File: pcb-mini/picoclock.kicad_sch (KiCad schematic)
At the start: 83 parts, among them J1 UART, J10 USB, J11 Alt Power, J12 LED_5V, J14 SJ2-35863B1-SMT-TR, J2 USB_A, J3 UART, J4 xx, J5 Micro_SD_Card_Det1, J6 USB_C_Receptacle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

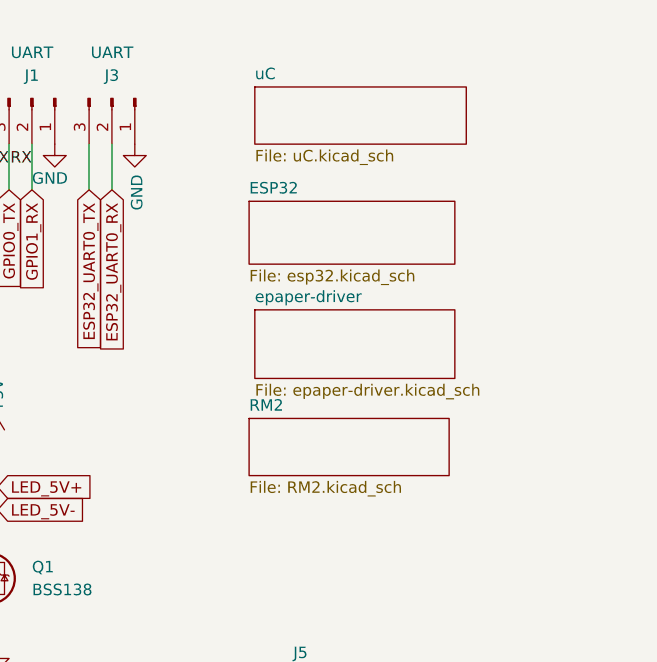
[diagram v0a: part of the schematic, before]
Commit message: [pcb] mini: add debug port, improve/fix traces
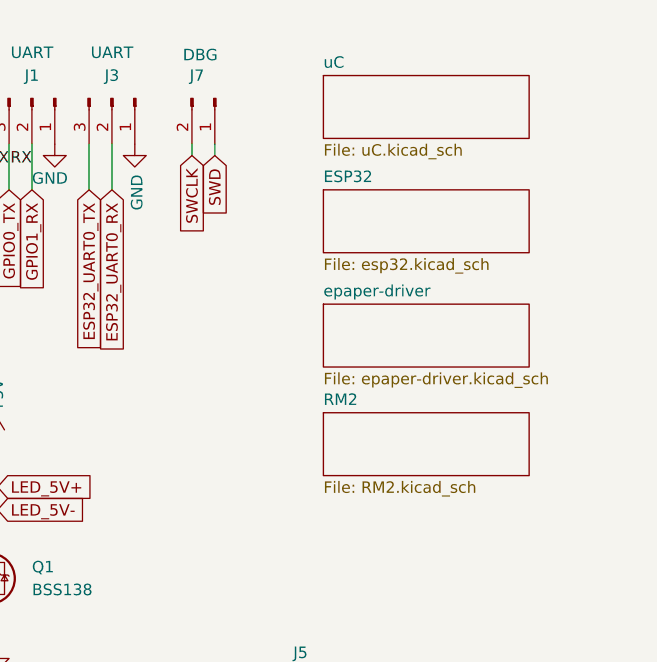
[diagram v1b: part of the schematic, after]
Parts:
- added J7: DBG, Connector_PinHeader_2.54mm:PinHeader_1x02_P2.54mm_Vertical, symbol Connector:Conn_01x02_Pin
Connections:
- new net SWCLK: J7.2 (Pin_2)
- new net SWD: J7.1 (Pin_1)
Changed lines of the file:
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@@
 	(wire
 		(pts
+			(xy 243.84 27.94) (xy 243.84 26.67)
+		)
+		(stroke
+			(width 0)
+			(type default)
+		)
+	)
+	(wire
+		(pts
 			(xy 31.75 166.37) (xy 31.75 171.45)
 		)
@@
 	(wire
 		(pts
+			(xy 241.3 27.94) (xy 241.3 26.67)
+		)
+		(stroke
+			(width 0)
+			(type default)
+		)
+	)
+	(wire
+		(pts
 			(xy 31.242 117.856) (xy 35.687 117.856)
 		)
@@
 		)
 	)
+	(global_label "SWCLK"
+		(shape input)
+		(at 241.3 27.94 270)
+		(fields_autoplaced yes)
+		(effects
+			(font
+				(size 1.27 1.27)
+			)
+			(justify right)
+		)
+		(property "Intersheetrefs" "${INTERSHEET_REFS}"
+			(at 241.3 37.1542 90)
+			(effects
+				(font
+					(size 1.27 1.27)
+				)
+				(justify right)
+				(hide yes)
+			)
+		)
+	)
 	(global_label "SDA"
 		(shape input)
@@
 		)
 	)
+	(global_label "SWD"
+		(shape input)
+		(at 243.84 27.94 270)
+		(fields_autoplaced yes)
+		(effects
+			(font
+				(size 1.27 1.27)
+			)
+			(justify right)
+		)
+		(property "Intersheetrefs" "${INTERSHEET_REFS}"
+			(at 243.84 34.8561 90)
+			(effects
+				(font
+					(size 1.27 1.27)
+				)
+				(justify right)
+				(hide yes)
+			)
+		)
+	)
 	(global_label "GPIO28{slash}btn"
 		(shape input)
@@
 	)
 	(symbol
+		(lib_id "Connector:Conn_01x02_Pin")
+		(at 243.84 21.59 270)
+		(unit 1)
+		(exclude_from_sim no)
+		(in_bom yes)
+		(on_board yes)
+		(dnp no)
+		(property "Reference" "J7"
+			(at 241.046 19.05 90)
+			(effects
+				(font
+					(size 1.27 1.27)
+				)
+				(justify left)
+			)
+		)
+		(property "Value" "DBG"
+			(at 240.284 16.764 90)
+			(effects
+				(font
+					(size 1.27 1.27)
+				)
+				(justify left)
+			)
+		)
+		(property "Footprint" "Connector_PinHeader_2.54mm:PinHeader_1x02_P2.54mm_Vertical"
+			(at 243.84 21.59 0)
+			(effects
+				(font
+					(size 1.27 1.27)
+				)
+				(hide yes)
+			)
+		)
+		(property "Datasheet" "~"
+			(at 243.84 21.59 0)
+			(effects
+				(font
+					(size 1.27 1.27)
+				)
+				(hide yes)
+			)
+		)
+		(property "Description" ""
+			(at 243.84 21.59 0)
+			(effects
+				(font
+					(size 1.27 1.27)
+				)
+				(hide yes)
+			)
+		)
+		(pin "1"
+		)
+		(pin "2"
+		)
+		(instances
+			(project "picoclock"
+				(path "/3b9dec0e-e0b7-4565-afc9-c4692f41aea9"
+					(reference "J7")
+					(unit 1)
+				)
+			)
+		)
+	)
+	(symbol
 		(lib_id "power:GND")
 		(at 76.327 107.696 90)
@@
 	)
 	(sheet
-		(at 247.65 33.02)
+		(at 255.905 31.75)
 		(size 22.86 6.985)
 		(exclude_from_sim no)
@@
 		)
 		(property "Sheetname" "ESP32"
-			(at 247.65 32.3084 0)
+			(at 255.905 31.0384 0)
 			(effects
 				(font
@@
 		)
 		(property "Sheetfile" "esp32.kicad_sch"
-			(at 247.65 40.5896 0)
+			(at 255.905 39.3196 0)
 			(effects
 				(font
@@
 	)
 	(sheet
-		(at 248.285 45.085)
-		(size 22.225 7.62)
+		(at 255.905 44.45)
+		(size 22.86 6.985)
 		(exclude_from_sim no)
 		(in_bom yes)
@@
 		)
 		(property "Sheetname" "epaper-driver"
-			(at 248.285 44.3734 0)
+			(at 255.905 43.7384 0)
 			(effects
 				(font
@@
 		)
 		(property "Sheetfile" "epaper-driver.kicad_sch"
-			(at 248.285 53.2896 0)
+			(at 255.905 52.0196 0)
 			(effects
 				(font
@@
 	)
 	(sheet
-		(at 247.65 57.15)
-		(size 22.225 6.35)
+		(at 255.905 56.515)
+		(size 22.86 6.985)
 		(exclude_from_sim no)
 		(in_bom yes)
@@
 		)
 		(property "Sheetname" "RM2"
-			(at 247.65 56.4384 0)
+			(at 255.905 55.8034 0)
 			(effects
 				(font
@@
 		)
 		(property "Sheetfile" "RM2.kicad_sch"
-			(at 247.65 64.0846 0)
+			(at 255.905 64.0846 0)
 			(effects
 				(font
@@
 	)
 	(sheet
-		(at 248.285 20.32)
-		(size 23.495 6.35)
+		(at 255.905 19.05)
+		(size 22.86 6.985)
 		(exclude_from_sim no)
 		(in_bom yes)
@@
 		)
 		(property "Sheetname" "uC"
-			(at 248.285 19.6084 0)
+			(at 255.905 18.3384 0)
 			(effects
 				(font
@@
 		)
 		(property "Sheetfile" "uC.kicad_sch"
-			(at 248.285 27.2546 0)
+			(at 255.905 26.6196 0)
 			(effects
 				(font

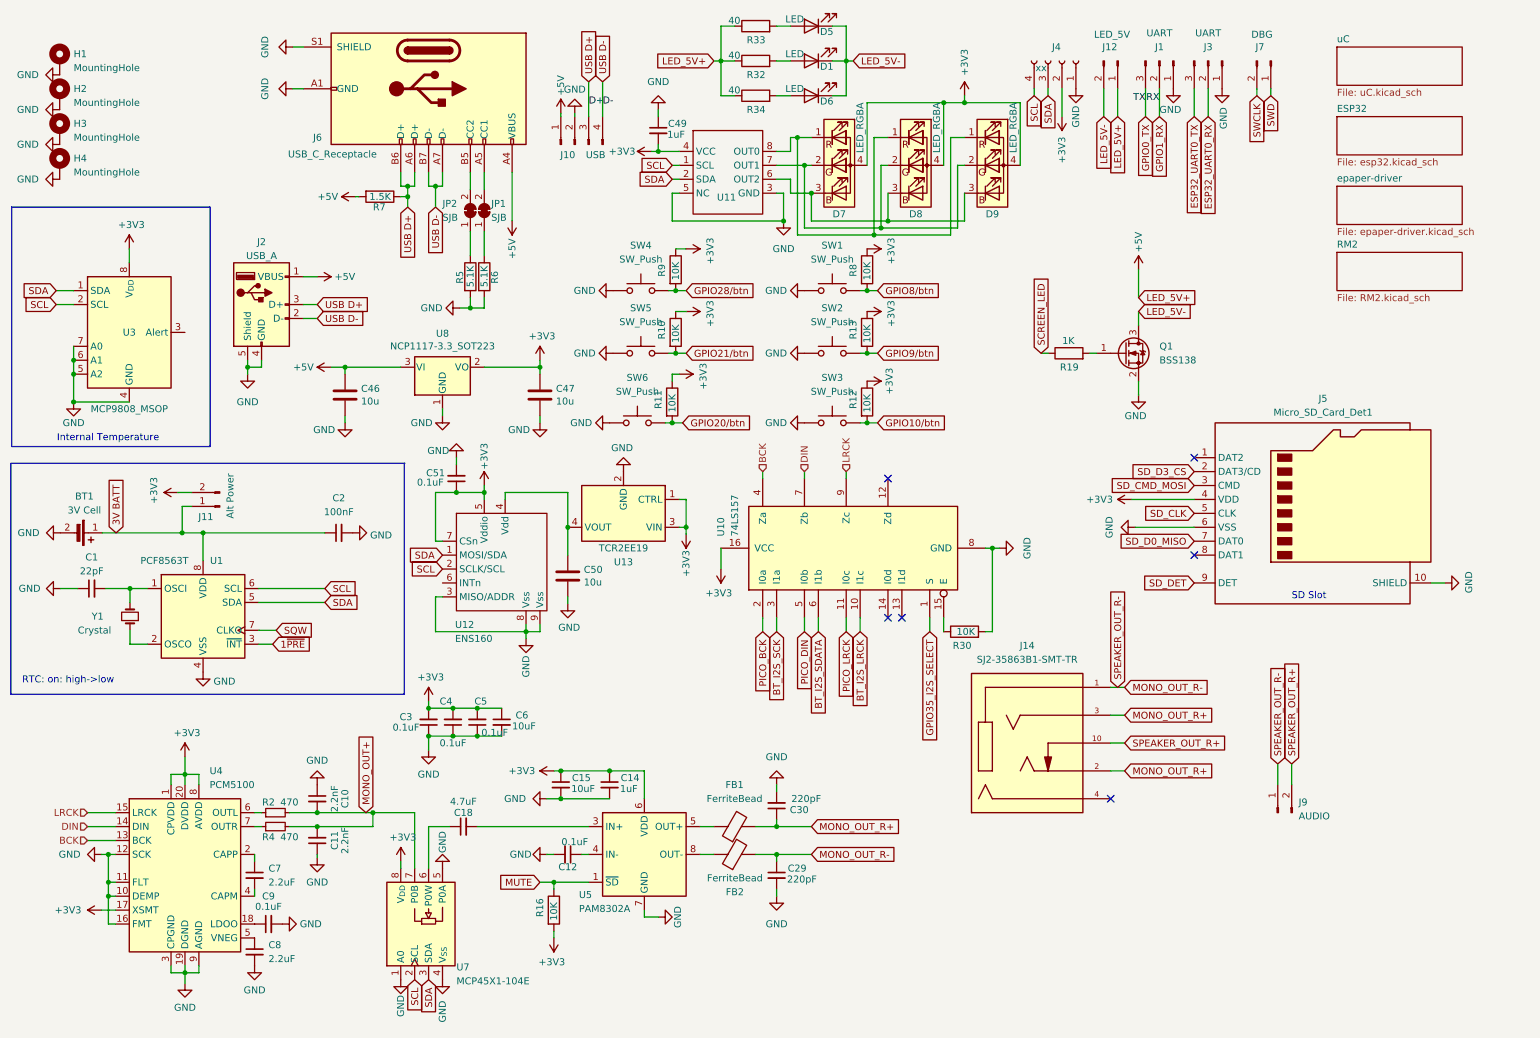
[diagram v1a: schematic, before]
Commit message: [pcb] mini: cleanup schematic, fix 3.3v zone
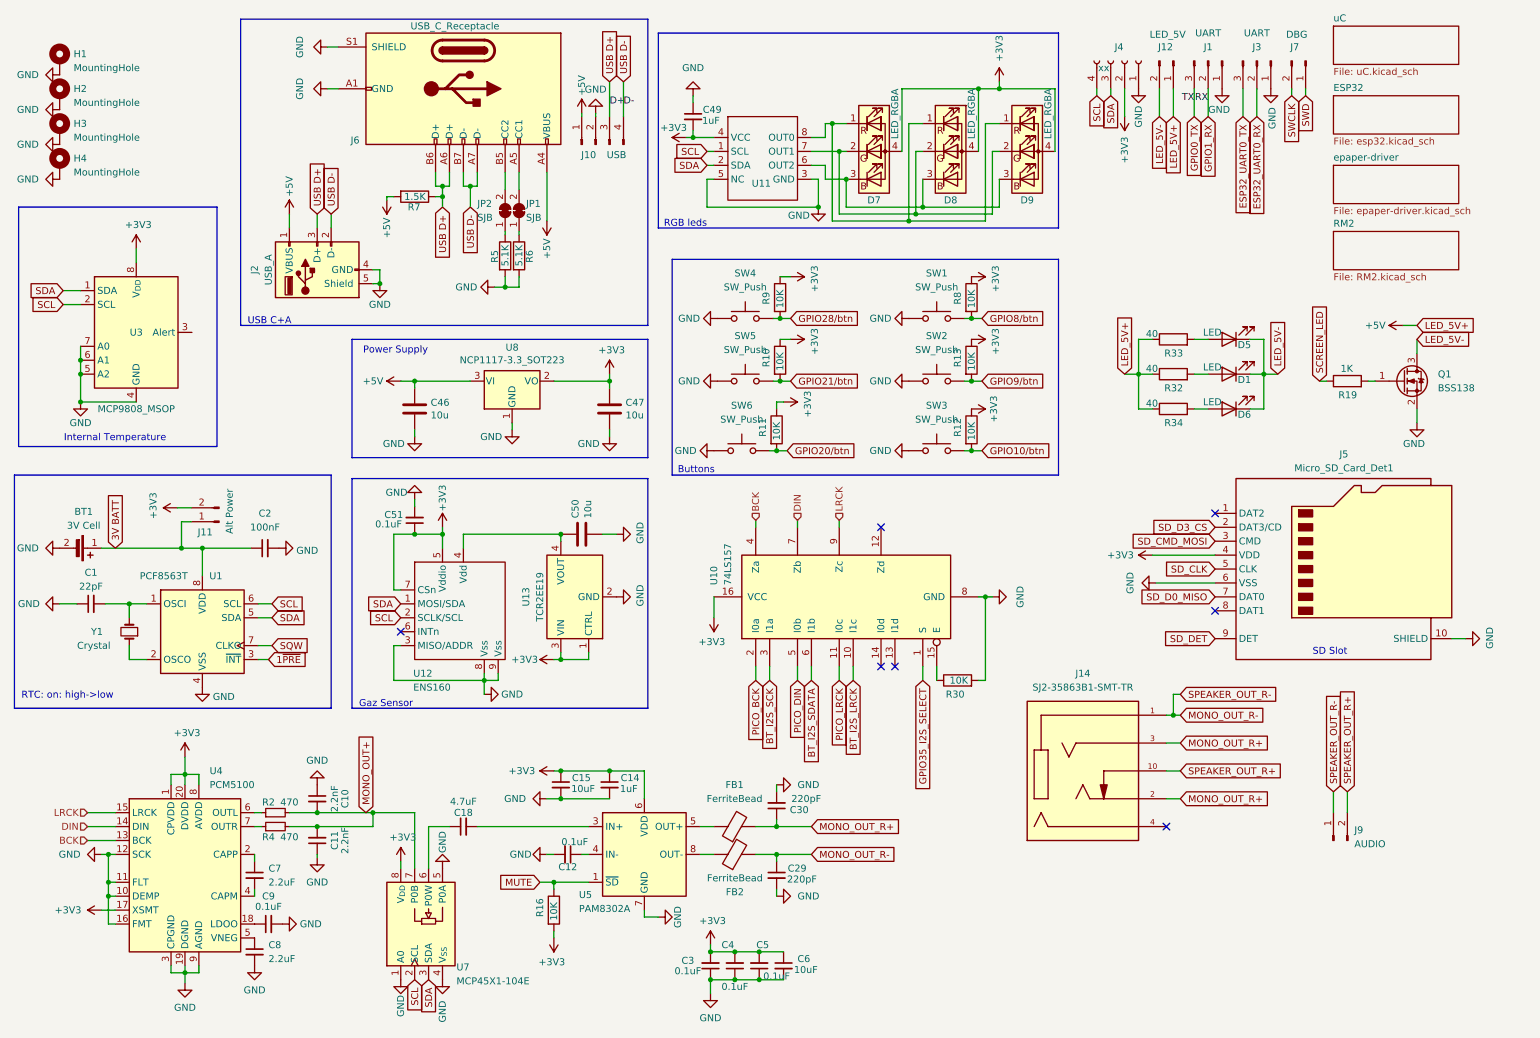
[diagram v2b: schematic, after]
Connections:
- no-connect marks 6 -> 7
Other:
- note added: "Buttons"
- note added: "Gaz Sensor"
- note added: "Power Supply"
- note added: "RGB leds"
- note added: "USB C+A"
- moved on the sheet: BT1, C1, C2, C3, C4, C46, C47, C49, C5, C50, C51, C6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

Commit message: [pcb] mini: add/fix LCSC refs
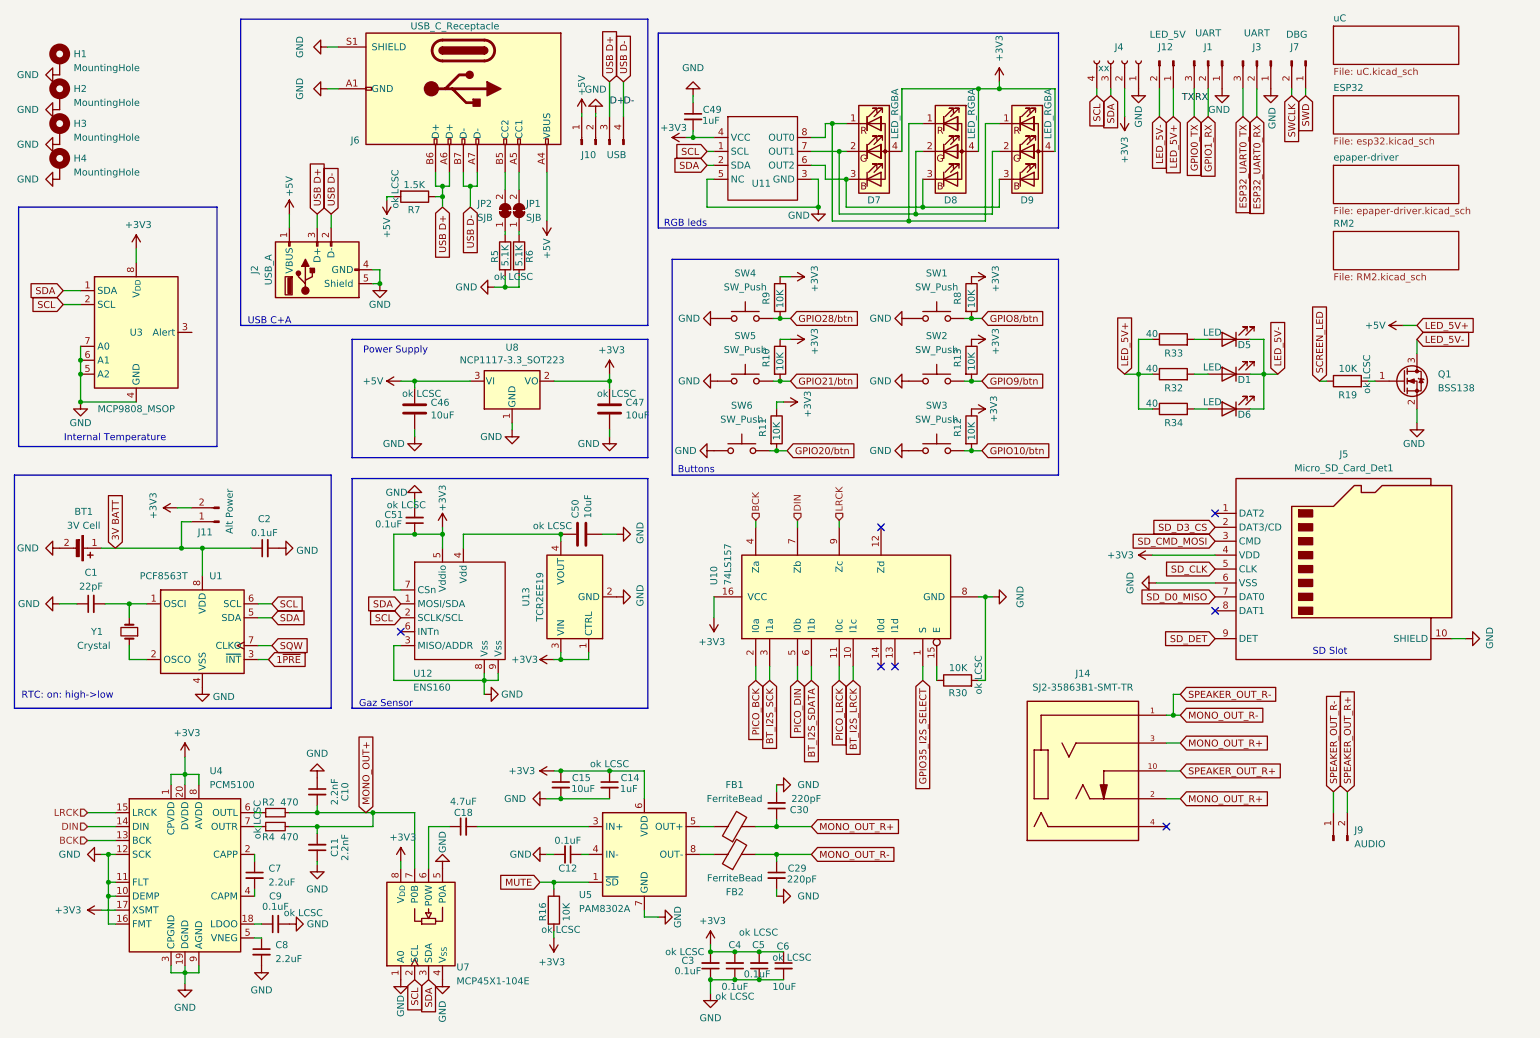
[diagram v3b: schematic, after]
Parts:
- C1: LCSC C1555 -> C1653
- C12, C3, C4, C5, C51, C9: LCSC (none) -> C14663
- C14: LCSC (none) -> C15849
- C2: value 100nF -> 0.1uF; LCSC C1525 -> C14663
- C46, C47, C50: value 10u -> 10uF; LCSC (none) -> C15850
- C6: LCSC (none) -> C15850
- Q1: footprint Package_TO_SOT_SMD:SOT-23 -> Package_TO_SOT_SMD:SOT-23-3
- R16, R30: footprint Resistor_SMD:R_0603_1608Metric -> Resistor_SMD:R_0402_1005Metric
- R19: value 1K -> 10K; footprint Resistor_SMD:R_0603_1608Metric -> Resistor_SMD:R_0402_1005Metric
- R2, R4: LCSC (none) -> C23179
- R5, R6: LCSC (none) -> C23186
- R7: LCSC (none) -> C22843
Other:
- moved on the sheet: C10, C11, C8, C9

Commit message: [pcb] mini: fix audio connector, resistor on 74LS157
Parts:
- removed R30: 10K, Resistor_SMD:R_0402_1005Metric, symbol Device:R
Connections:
- net GND: now also U10.15 (E)
- net GPIO35_I2S_SELECT renamed GPIO38_I2S_SELECT
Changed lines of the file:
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@@
 	(wire
 		(pts
+			(xy 182.88 133.35) (xy 191.77 133.35)
+		)
+		(stroke
+			(width 0)
+			(type default)
+		)
+	)
+	(wire
+		(pts
 			(xy 165.1 134.62) (xy 165.1 132.08)
 		)
@@
 	(wire
 		(pts
-			(xy 190.5 134.62) (xy 191.77 134.62)
-		)
-		(stroke
-			(width 0)
-			(type default)
-		)
-	)
-	(wire
-		(pts
 			(xy 240.03 78.74) (xy 242.57 78.74)
 		)
@@
 	(wire
 		(pts
-			(xy 191.77 134.62) (xy 191.77 119.38)
+			(xy 191.77 133.35) (xy 191.77 119.38)
 		)
 		(stroke
@@
 	(wire
 		(pts
-			(xy 182.88 134.62) (xy 182.88 132.08)
+			(xy 182.88 133.35) (xy 182.88 132.08)
 		)
 		(stroke
@@
 		)
 	)
-	(global_label "GPIO35_I2S_SELECT"
+	(global_label "GPIO38_I2S_SELECT"
 		(shape input)
 		(at 180.34 134.62 270)
@@
 					(unit 1)
 				)
-			)
-		)
-	)
-	(symbol
-		(lib_id "Device:R")
-		(at 186.69 134.62 90)
-		(unit 1)
-		(exclude_from_sim no)
-		(in_bom yes)
-		(on_board yes)
-		(dnp no)
-		(property "Reference" "R30"
-			(at 188.468 136.906 90)
-			(effects
-				(font
-					(size 1.27 1.27)
-				)
-				(justify left)
-			)
-		)
-		(property "Value" "10K"
-			(at 188.468 132.334 90)
-			(effects
-				(font
-					(size 1.27 1.27)
-				)
-				(justify left)
-			)
-		)
-		(property "Footprint" "Resistor_SMD:R_0402_1005Metric"
-			(at 186.69 136.398 90)
-			(effects
-				(font
-					(size 1.27 1.27)
-				)
-				(hide yes)
-			)
-		)
-		(property "Datasheet" "~"
-			(at 186.69 134.62 0)
-			(effects
-				(font
-					(size 1.27 1.27)
-				)
-				(hide yes)
-			)
-		)
-		(property "Description" "ok LCSC"
-			(at 190.5 133.604 0)
-			(effects
-				(font
-					(size 1.27 1.27)
-				)
-			)
-		)
-		(property "LCSC" "C25744"
-			(at 186.69 134.62 0)
-			(effects
-				(font
-					(size 1.27 1.27)
-				)
-				(hide yes)
-			)
-		)
-		(pin "1"
-		)
-		(pin "2"
-		)
-		(instances
-			(project "picoclock"
-				(path "/3b9dec0e-e0b7-4565-afc9-c4692f41aea9"
-					(reference "R30")
-					(unit 1)
-				)

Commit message: [pcb] mini: RGB led footprint fixes
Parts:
- D7, D8, D9: footprint Resistor_SMD:R_Array_Convex_2x0606 -> LED_SMD:LED_LiteOn_LTST-C19HE1WT
- U13: footprint Package_TO_SOT_SMD:SOT-23-5_HandSoldering -> Package_TO_SOT_SMD:SC-74A-5_1.55x2.9mm_P0.95mm
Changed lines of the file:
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@@
 			)
 		)
-		(property "Footprint" "Package_TO_SOT_SMD:SOT-23-5_HandSoldering"
+		(property "Footprint" "Package_TO_SOT_SMD:SC-74A-5_1.55x2.9mm_P0.95mm"
 			(at 127 119.38 0)
 			(effects
@@
 			)
 		)
-		(property "Footprint" "Resistor_SMD:R_Array_Convex_2x0606"
+		(property "Footprint" "LED_SMD:LED_LiteOn_LTST-C19HE1WT"
 			(at 185.42 39.37 0)
 			(effects
@@
 			)
 		)
-		(property "Footprint" "Resistor_SMD:R_Array_Convex_2x0606"
+		(property "Footprint" "LED_SMD:LED_LiteOn_LTST-C19HE1WT"
 			(at 171.45 39.37 0)
 			(effects
@@
 			)
 		)
-		(property "Footprint" "Resistor_SMD:R_Array_Convex_2x0606"
+		(property "Footprint" "LED_SMD:LED_LiteOn_LTST-C19HE1WT"
 			(at 199.39 39.37 0)
 			(effects
